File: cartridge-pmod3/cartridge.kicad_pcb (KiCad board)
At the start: 2 copper layers, 64.8 x 55.9 mm, 17 parts, among them J1 Cartridge Connector, U1 W25Q128, U2 S70KL1281-pkl_memory

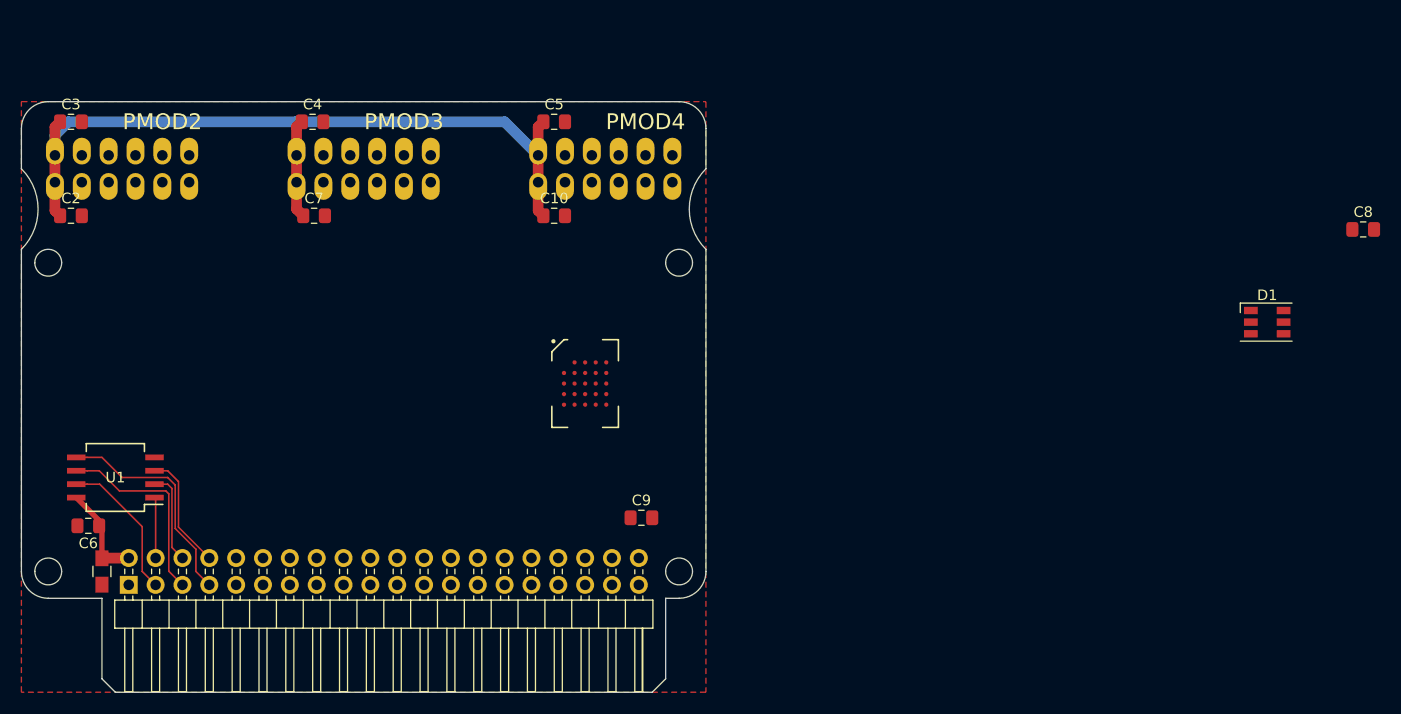
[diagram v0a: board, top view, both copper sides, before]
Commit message: cartridge-pmod3 : routed and placed, pmod4 pending, DRC errors to resolve
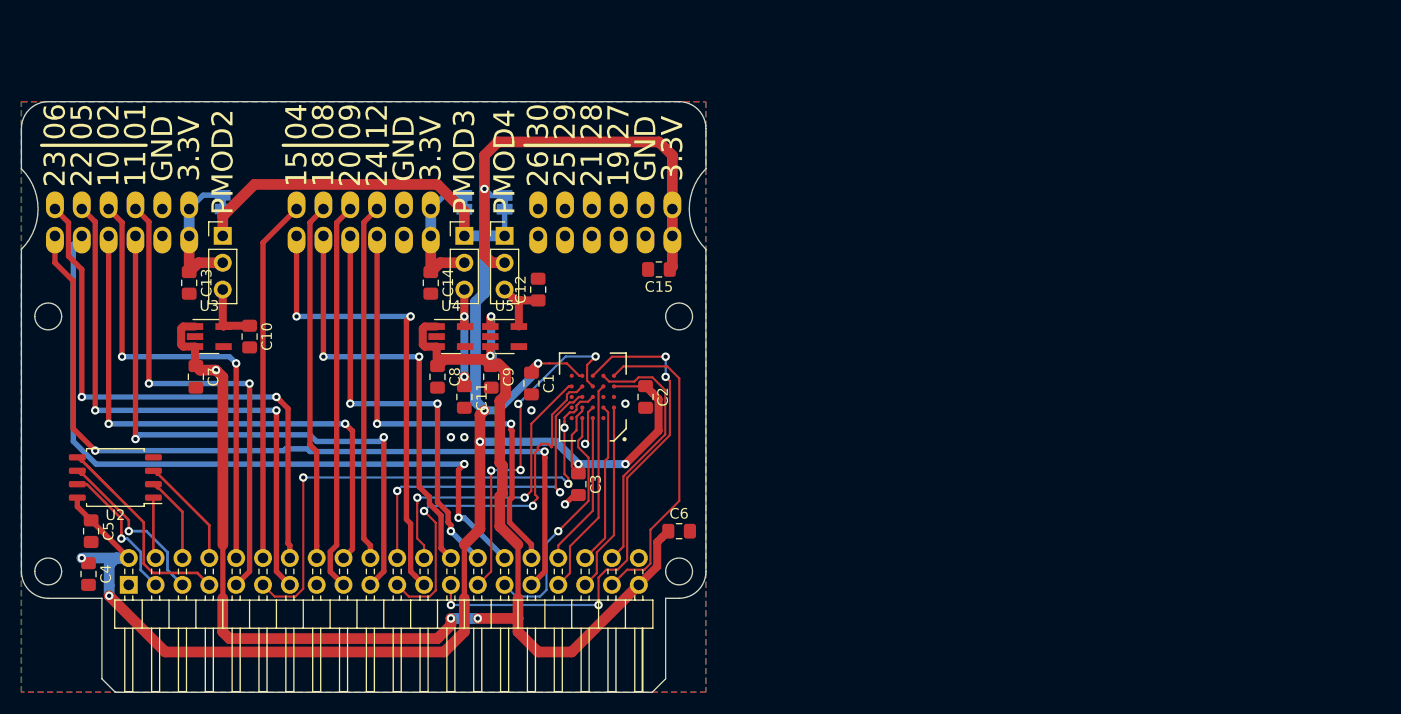
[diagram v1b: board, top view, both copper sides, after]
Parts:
- removed D1: APA102, tom-semiconductors:LED_RGB_PLCC-6
- added C11: 1uF/10V, tom-passives:C_0805_2012Metric_Pad1.15x1.40mm_HandSolder, F.Cu at (109.2, 78.7)
- added C12: 1uF/10V, tom-passives:C_0805_2012Metric_Pad1.15x1.40mm_HandSolder, F.Cu at (116.2, 68.6)
- added C13: 10uF/10V, tom-passives:C_0805_2012Metric_Pad1.15x1.40mm_HandSolder, F.Cu at (83.2, 67.9)
- added C14: 10uF/10V, tom-passives:C_0805_2012Metric_Pad1.15x1.40mm_HandSolder, F.Cu at (106.0, 67.9)
- added C15: 10uF/10V, tom-passives:C_0805_2012Metric_Pad1.15x1.40mm_HandSolder, F.Cu at (127.6, 66.7)
- added JP1: JUMPER3, tom-connectors:PinHeader_1x03_P2.54mm_Vertical, F.Cu at (113.0, 63.5)
- added JP2: JUMPER3, tom-connectors:PinHeader_1x03_P2.54mm_Vertical, F.Cu at (86.4, 63.5)
- added JP3: JUMPER3, tom-connectors:PinHeader_1x03_P2.54mm_Vertical, F.Cu at (109.2, 63.5)
- added JP4: JUMPER, tom-mechanical:SolderJumper-2_P1.3mm_Bridged_Pad1.0x1.5mm, B.Cu at (86.4, 60.3)
- added JP5: JUMPER, tom-mechanical:SolderJumper-2_P1.3mm_Bridged_Pad1.0x1.5mm, B.Cu at (109.2, 60.3)
- added JP6: JUMPER, tom-mechanical:SolderJumper-2_P1.3mm_Bridged_Pad1.0x1.5mm, B.Cu at (113.0, 60.3)
- added U3: AP2112K-3.3, tom-semiconductors:SOT-23-5_HandSoldering, F.Cu at (85.1, 73.0)
- added U4: AP2112K-3.3, tom-semiconductors:SOT-23-5_HandSoldering, F.Cu at (108.0, 73.0)
- added U5: AP2112K-3.3, tom-semiconductors:SOT-23-5_HandSoldering, F.Cu at (113.0, 73.0)
- C1: footprint Capacitors_SMD:C_0805_HandSoldering -> tom-passives:C_0805_2012Metric_Pad1.15x1.40mm_HandSolder
- C10, C7, C8: value 10uF -> 1uF/10V
- C2: value 10uF -> 100nF
- C4: value 100nF -> 10uF
- C6: value 10uF -> 10uF/10V
- C9: value 100nF -> 1uF/10V
- U1: value W25Q128 -> S70KL1281-pkl_memory; footprint Housings_SOIC:SO-8_5.3x6.2mm_Pitch1.27mm -> tom-semiconductors:BGA-24_5x5_6.0x8.0mm
- U2: value S70KL1281-pkl_memory -> W25Q128; footprint tom-semiconductors:BGA-24_5x5_6.0x8.0mm -> tom-semiconductors:SOIC-8_5.23x5.23mm_P1.27mm
- moved C8 88.7 mm to (106.7, 76.8), turned to 270 degrees
- moved C3 59.0 mm to (120.0, 87.0), turned to 270 degrees
- moved C5 58.5 mm to (73.9, 91.4), turned to 270 degrees
- moved C2 57.0 mm to (126.4, 78.7), turned to 270 degrees
- moved C6 55.9 mm to (129.5, 91.4), turned to 0 degrees
- moved C4 47.8 mm to (73.7, 95.5), turned to 270 degrees
- moved U1 45.8 mm to (121.4, 78.7)
- moved U2 45.3 mm to (76.2, 86.4), turned to 180 degrees
- moved C1 44.4 mm to (115.6, 77.5)
- moved C10 31.0 mm to (88.9, 73.0), turned to 270 degrees
- moved C9 19.5 mm to (111.8, 76.8), turned to 270 degrees
- moved C7 18.9 mm to (83.8, 76.8), turned to 270 degrees
- moved PMOD2 5.08 mm to (76.8, 62.2), turned to 180 degrees
- moved PMOD3 5.08 mm to (99.7, 62.2), turned to 180 degrees
- moved PMOD4 5.08 mm to (122.6, 62.2), turned to 180 degrees
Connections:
- C10 pad 1: +3V3 -> /3V3-A
- C6 pad 1: +3V3 -> +5V
- C7 pad 1: +3V3 -> +5V
- J1 pad 15: GENIO7_PT6B -> (no net)
- J1 pad 40: Net-(J1-Pad40) -> (no net)
- PMOD2 pad 12: +3V3 -> /3V3-PMOD2
- PMOD2 pad 6: +3V3 -> /3V3-PMOD2
- PMOD3 pad 12: +3V3 -> /3V3-PMOD3
- PMOD3 pad 6: +3V3 -> /3V3-PMOD3
- PMOD4 pad 1: GENIO30_PT56B -> (no net)
- PMOD4 pad 10: GENIO19_PT33B -> (no net)
- PMOD4 pad 12: +3V3 -> /3V3-PMOD4
- PMOD4 pad 2: GENIO29_PR14B -> (no net)
- PMOD4 pad 3: GENIO28_PT49A -> (no net)
- PMOD4 pad 4: GENIO27_PT44A -> (no net)
- PMOD4 pad 6: +3V3 -> /3V3-PMOD4
- PMOD4 pad 7: GENIO26_PR20B -> (no net)
- PMOD4 pad 8: GENIO25_PR17B -> (no net)
- PMOD4 pad 9: GENIO21_PT42A -> (no net)
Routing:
- net +5V: track 0.00 -> 129.0 mm, vias 0 -> 5
- net +3V3: track 90.0 -> 181.1 mm, vias 0 -> 7
- net GENIO23_PT38A_P: track 0.00 -> 77.7 mm, vias 0 -> 2
- net GENIO22_PT38B_N: track 0.00 -> 68.9 mm, vias 0 -> 2
- net GENIO11_PT15B_N: track 0.00 -> 57.8 mm, vias 0 -> 2
- net GENIO5_PT4B_N: track 0.00 -> 53.8 mm, vias 0 -> 2
- net GENIO10_PT15A_P: track 0.00 -> 53.5 mm, vias 0 -> 2
- net GENIO6_PT4A_P: track 0.00 -> 53.0 mm, vias 0 -> 2
- net GENIO17_PT29A: track 0.00 -> 50.6 mm, vias 0 -> 4
- net GENIO3_PL11B: track 0.00 -> 50.6 mm, vias 0 -> 3
- net GENIO1_PL11D_N: track 0.00 -> 46.2 mm, vias 0 -> 2
- net GENIO15_PT31A_P: track 0.00 -> 44.7 mm, vias 0 -> 2
- net GENIO24_PT36B_N: track 0.00 -> 44.2 mm, vias 0 -> 2
- net GENIO2_PL11C_P: track 0.00 -> 44.0 mm, vias 0 -> 2
- net /3V3-PMOD4: track 0.00 -> 43.5 mm, vias 0 -> 1
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- added copper zone on B.Cu, net GND
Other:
- outline, holes or cut-outs redrawn
- board text added: "01"
- board text added: "02"
- board text added: "04"
- board text added: "05"
- board text added: "06"
- board text added: "08"
- board text added: "09"
- board text added: "10"
- board text added: "11"
- board text added: "12"
- board text added: "15"
- board text added: "18"
- board text added: "19"
- board text added: "20"
- board text added: "21"
- board text added: "22"
- board text added: "23"
- board text added: "24"
- board text added: "25"
- board text added: "26"
- board text added: "27"
- board text added: "28"
- board text added: "29"
- board text added: "3"
- board text added: "3.3V"
- board text added: "30"
- board text added: "GND"
- board text added: "PCB by tom@tomk.in"
- board text added: "PMOD"
- board text added: "Template by Thomas Flummer"

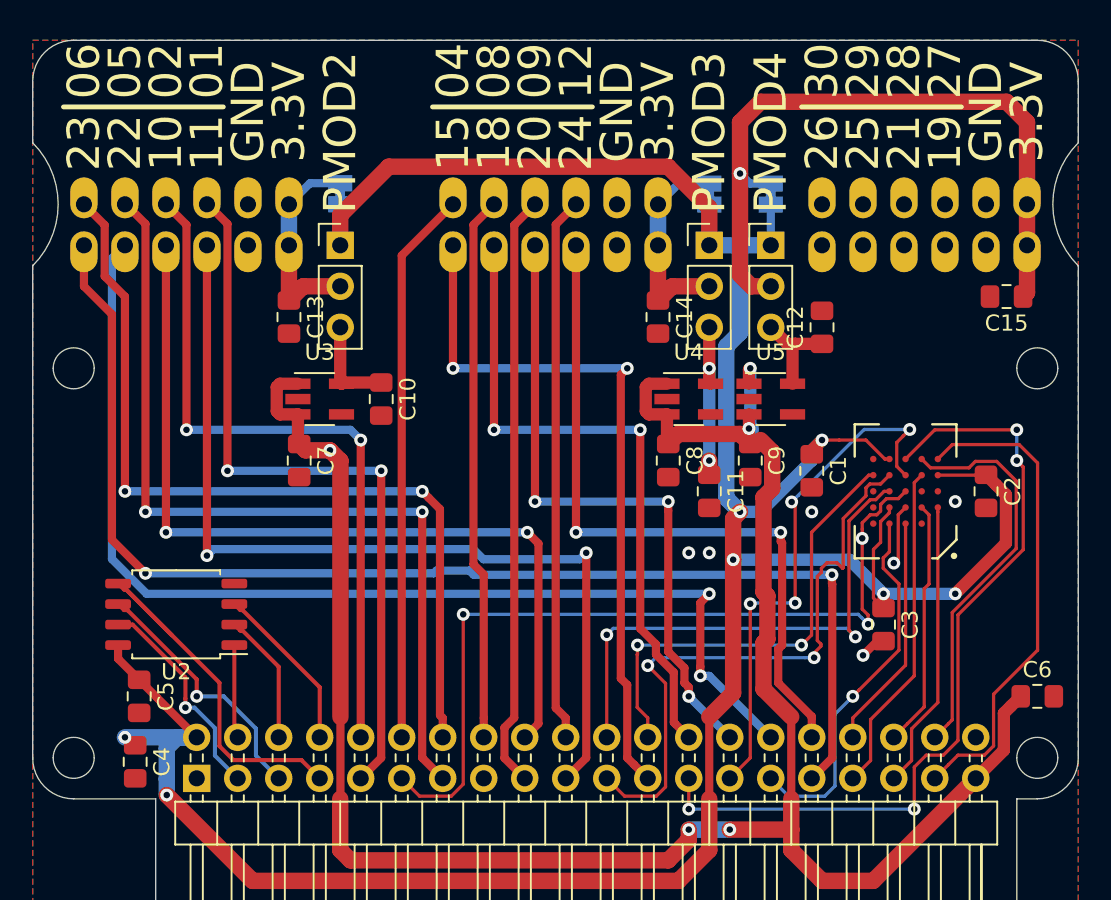
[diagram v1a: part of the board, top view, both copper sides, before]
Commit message: cartridge-pmod3 : routed, fixed silk, pending board resize
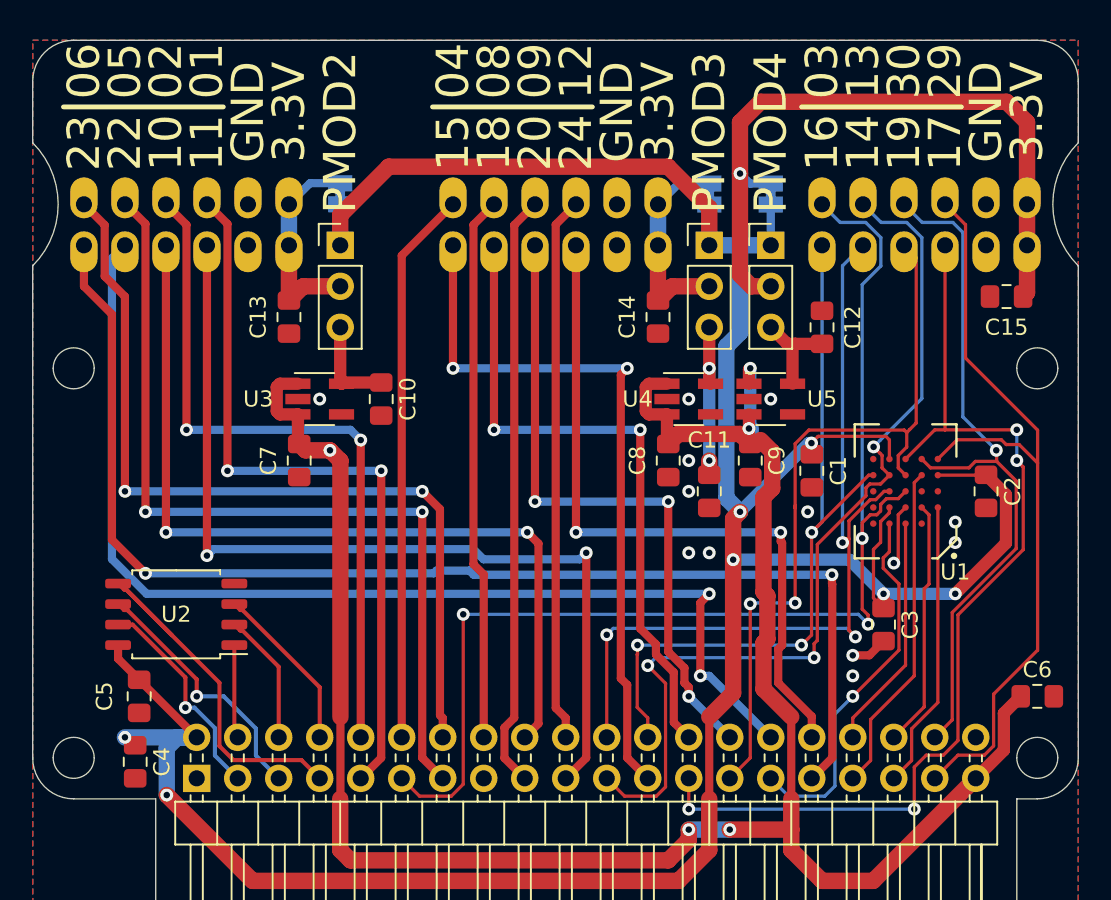
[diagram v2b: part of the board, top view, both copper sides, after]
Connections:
- PMOD4 pad 1: (no net) -> GENIO3_PL11B
- PMOD4 pad 10: (no net) -> GENIO17_PT29A
- PMOD4 pad 2: (no net) -> GENIO13_PT20A
- PMOD4 pad 3: (no net) -> GENIO30_PT56B
- PMOD4 pad 4: (no net) -> GENIO29_PR14B
- PMOD4 pad 7: (no net) -> GENIO16_PT33A
- PMOD4 pad 8: (no net) -> GENIO14_PT27A
- PMOD4 pad 9: (no net) -> GENIO19_PT33B
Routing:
- net GENIO3_PL11B: track 50.6 -> 74.2 mm
- net GENIO13_PT20A: track 37.8 -> 57.3 mm, vias 2 -> 3
- net GENIO14_PT27A: track 32.8 -> 52.2 mm, vias 2 -> 3
- net GENIO30_PT56B: track 24.7 -> 44.1 mm, vias 0 -> 1
- net GENIO29_PR14B: track 30.2 -> 48.8 mm
- net GENIO16_PT33A: track 28.7 -> 46.7 mm, vias 2 -> 3
- net GENIO19_PT33B: track 33.1 -> 46.7 mm, vias 4 -> 2
- net GENIO17_PT29A: track 50.6 -> 62.0 mm
- net GND: track 5.38 -> 6.41 mm, vias 6 -> 13
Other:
- board text added: "03"
- board text added: "13"
- board text added: "14"
- board text added: "16"
- board text added: "17"
- board text removed: "21"
- board text removed: "25"
- board text removed: "26"
- board text removed: "27"
- board text removed: "28"

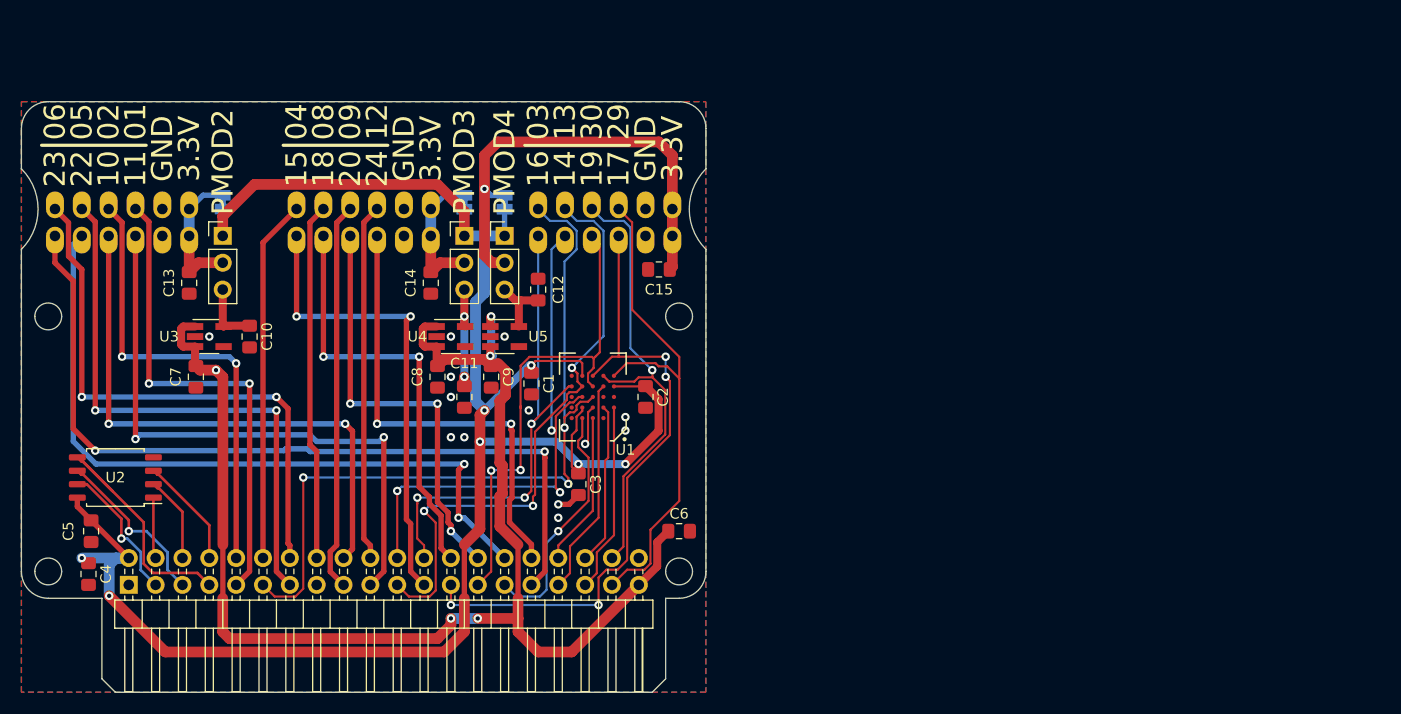
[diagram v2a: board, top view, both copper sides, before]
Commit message: cartridge-pmod3:Add LICENSE cartridge-pmod3:adjust size to match pmod 3d model
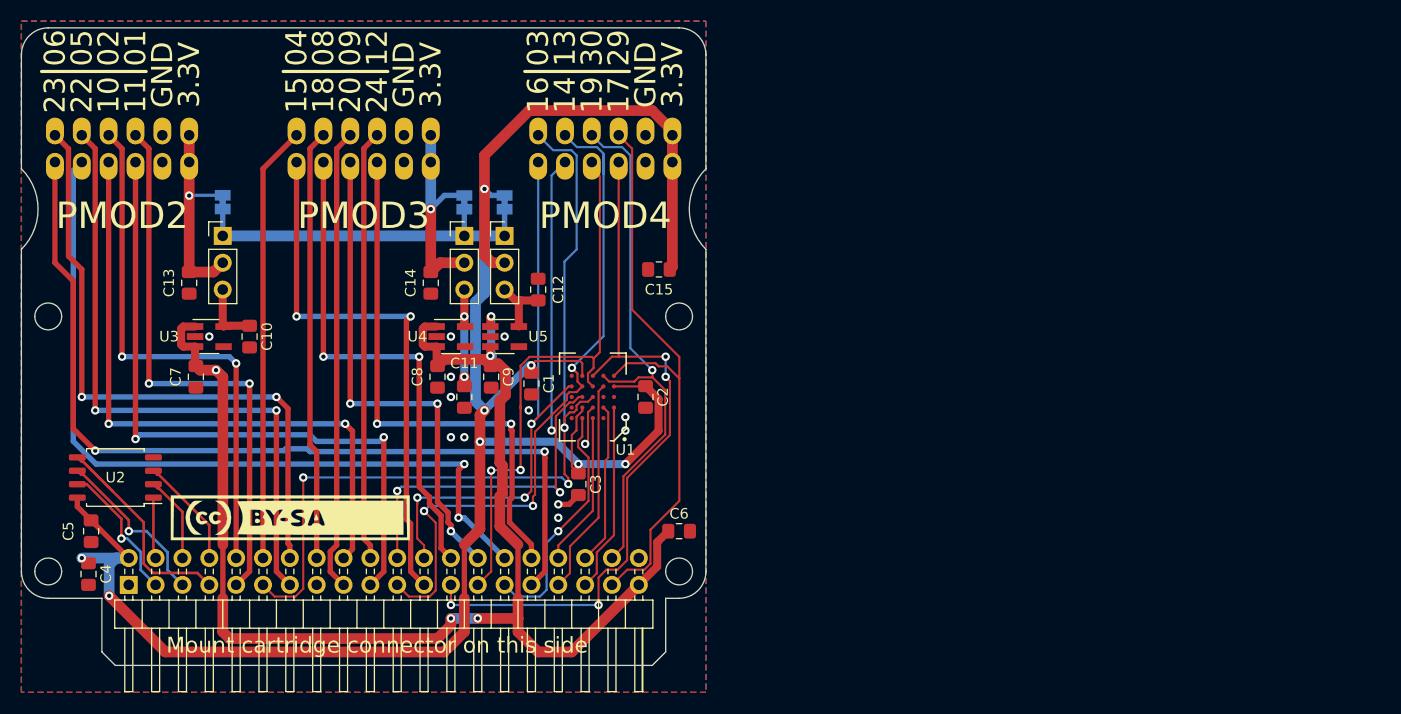
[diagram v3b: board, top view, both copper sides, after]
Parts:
- added G***: LOGO, tom-mechanical:cc-by-sa-80x15, F.Cu at (92.7, 90.2)
- moved PMOD2 6.98 mm to (76.8, 55.2)
- moved PMOD3 6.98 mm to (99.7, 55.2)
- moved PMOD4 6.98 mm to (122.6, 55.2)
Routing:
- net GENIO13_PT20A: track 57.3 -> 66.2 mm
- net GENIO3_PL11B: track 74.2 -> 81.3 mm
- net GENIO9_PT18A_P: track 36.9 -> 43.9 mm
- net GENIO6_PT4A_P: track 53.0 -> 60.0 mm
- net GENIO23_PT38A_P: track 77.7 -> 84.7 mm
- net GENIO22_PT38B_N: track 68.9 -> 75.9 mm
- net GENIO12_PT18B_N: track 33.8 -> 40.8 mm
- net /3V3-PMOD3: track 13.2 -> 20.2 mm, vias 0 -> 1
- net GENIO8_PT11B_N: track 33.8 -> 40.8 mm
- net GENIO4_PT11A_P: track 34.3 -> 41.3 mm
- net GENIO2_PL11C_P: track 44.0 -> 51.0 mm
- net GENIO29_PR14B: track 48.8 -> 55.8 mm
- net GENIO24_PT36B_N: track 44.2 -> 51.1 mm
- net GENIO20_PT36A_P: track 40.3 -> 47.3 mm
- net GENIO18_PT31B_N: track 40.8 -> 47.8 mm
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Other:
- board size 64.8 x 55.9 mm -> 64.8 x 60.3 mm
- board text added: "Mount PMOD Connectors on this side facing this edge"
- board text added: "Mount cartridge connector on this side"
- board text added: "template by Thomas Flummer"
- board text added: "tom@tomk.in v1.0"
- board text removed: "Mount PMOD Connectors on this side"
- board text removed: "PCB by tom@tomk.in"
- board text removed: "Template by Thomas Flummer"

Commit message: cartridge-pmod3:fix silk
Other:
- board text removed: "template by Thomas Flummer"
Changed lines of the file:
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@@
   (general
     (thickness 1.6)
-    (drawings 76)
+    (drawings 75)
     (tracks 539)
     (zones 0)
@@
   )
   (setup
-    (last_trace_width 0.508)
+    (last_trace_width 0.1524)
     (user_trace_width 0.2032)
     (user_trace_width 0.254)
@@
     (effects (font (size 2 2) (thickness 0.3)) (justify mirror))
   )
-  (gr_text "template by\nThomas Flummer" (at 114.935 100.33) (layer B.SilkS)
-    (effects (font (size 2 2) (thickness 0.3)) (justify mirror))
-  )
